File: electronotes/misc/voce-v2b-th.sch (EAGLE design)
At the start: 94 parts, among them IC1 LM13700, IC11 LM13700, IC14 LM13700, IC16 TL072, IC2 LM13700, IC3 LM13700, IC5 TL074, IC6 TL072, IC7 TL072

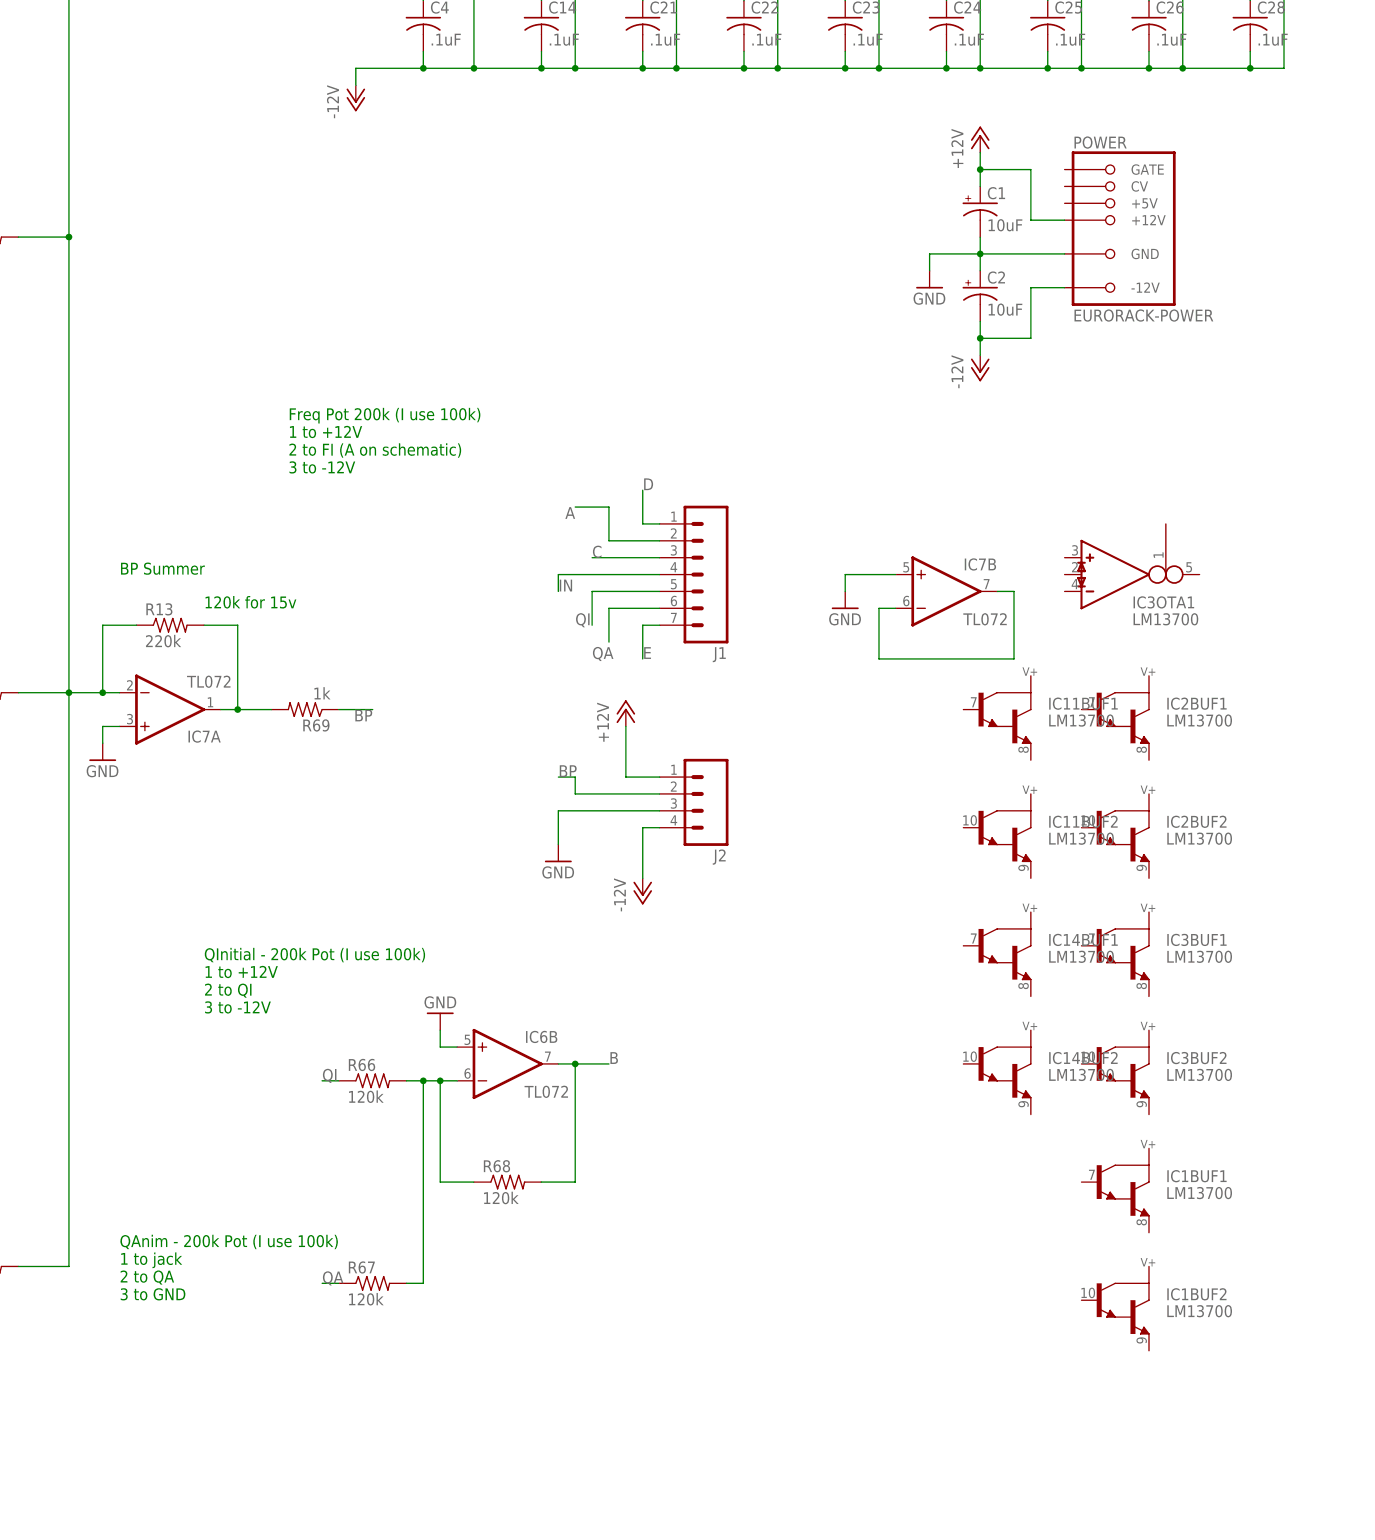
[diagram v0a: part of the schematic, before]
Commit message: Add pot symbols to make things clearer.
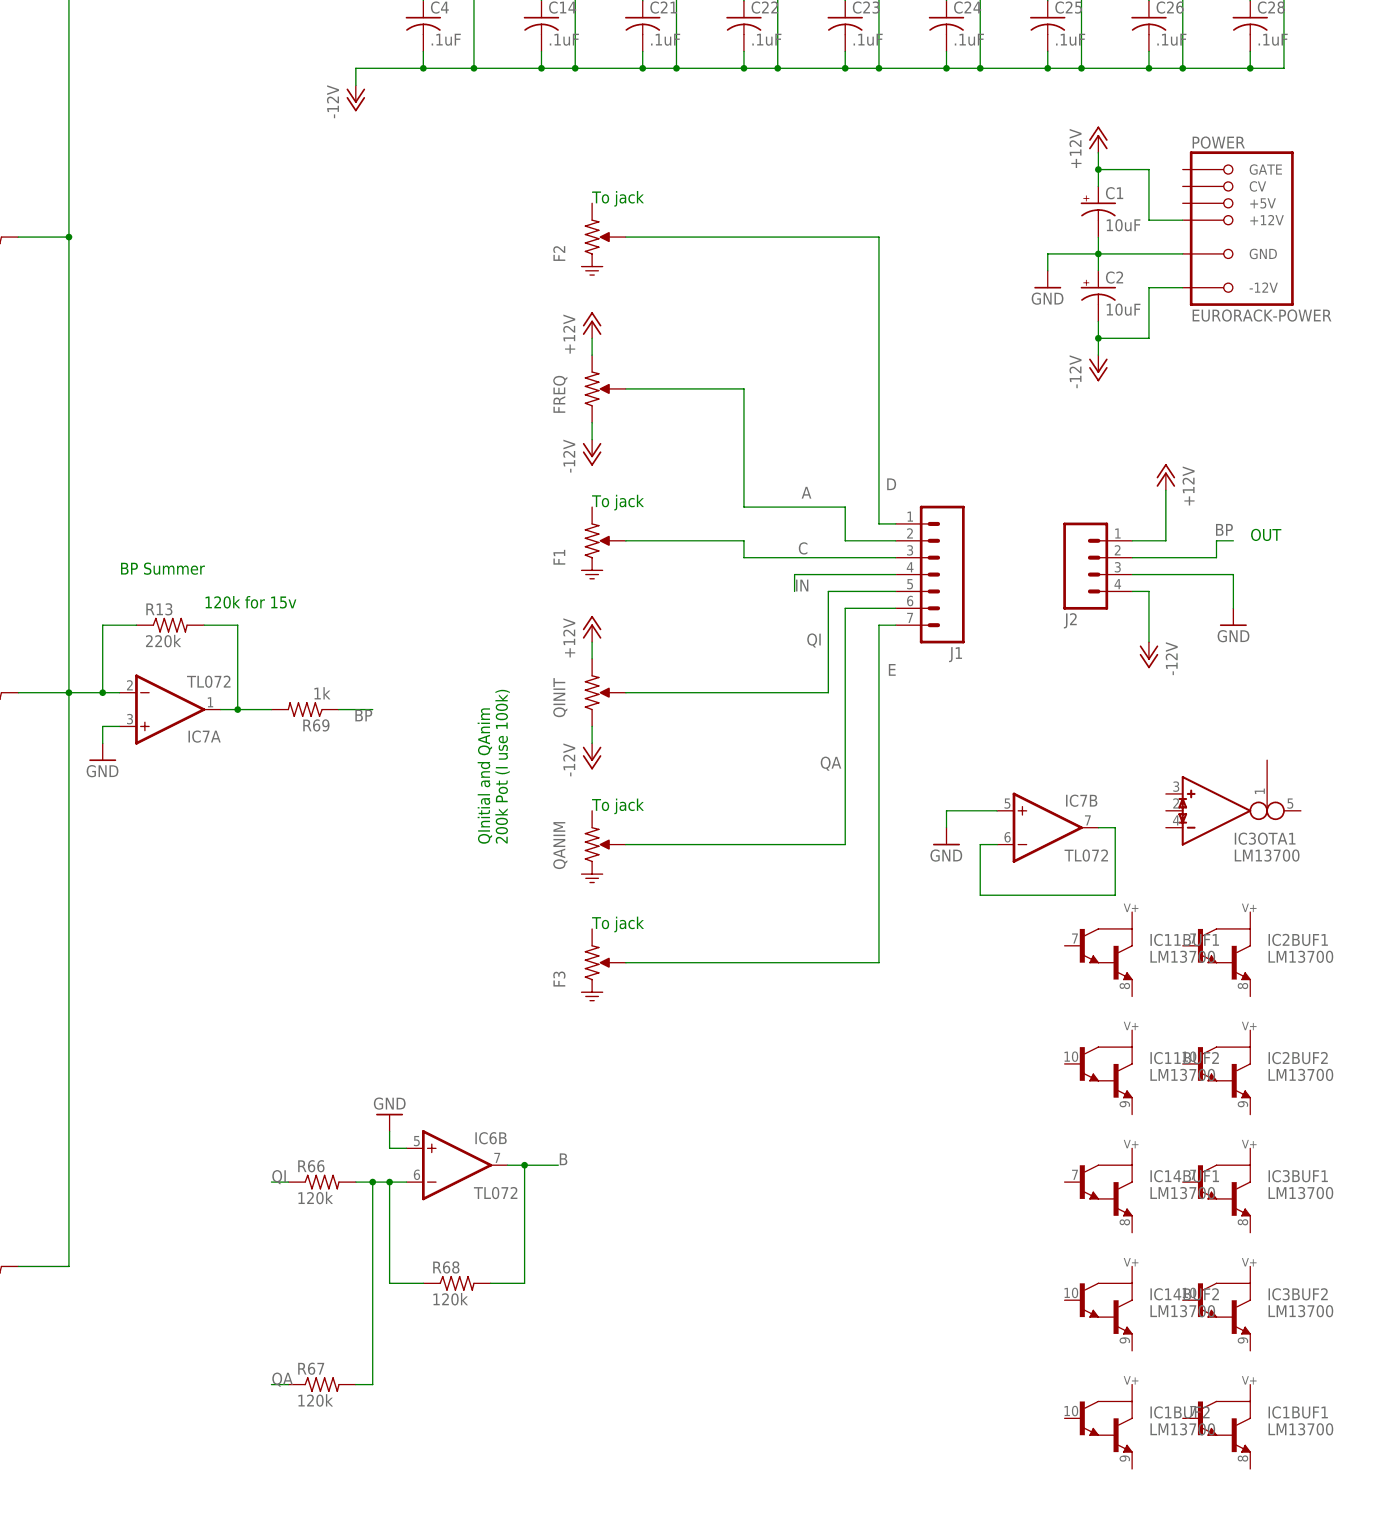
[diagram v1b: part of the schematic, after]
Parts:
- added F1, F2, F3, QANIM: (no value), mmoretti:POT-ATTEN
- added FREQ, QINIT: (no value), mmoretti:POT
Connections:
- net +12V: now also FREQ.1, QINIT.1
- net -12V: now also FREQ.3, QINIT.3
- net A: now also FREQ.2
- net C: now also F1.2
- net D: now also F2.2
- net E: now also F3.2
- net QA: now also QANIM.2
- net QI: now also QINIT.2
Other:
- note added: "OUT"
- note added: "QInitial and QAnim 200k Pot (I use 100k)"
- note added: "To jack"
- note removed: "Freq Pot 200k (I use 100k) 1 to +12V 2 to FI (A on schematic) 3 to -12V"
- note removed: "QAnim - 200k Pot (I use 100k) 1 to jack 2 to QA 3 to GND"
- note removed: "QInitial - 200k Pot (I use 100k) 1 to +12V 2 to QI 3 to -12V"
- moved on the sheet: C1, C2, IC11BUF1, IC11BUF2, IC14BUF1, IC14BUF2, IC1BUF1, IC1BUF2, IC2BUF1, IC2BUF2, IC3BUF1, IC3BUF2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
